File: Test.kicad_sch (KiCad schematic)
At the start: 1 part, among them U1 14528

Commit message: Updated KiCad project files with new changes
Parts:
- removed U1: 14528, symbol 4xxx:14528
- added U1, U10, U3, U4, U5, U6, U7, U8, U9: ADG1207YCPZ-REEL7, CP_32_2_ADI, symbol ADG_new:ADG1207YCPZ-REEL7
- added U2: ADL5308ACCZ, CC-14-4_ADI, symbol ADL_new:ADL5308ACCZ

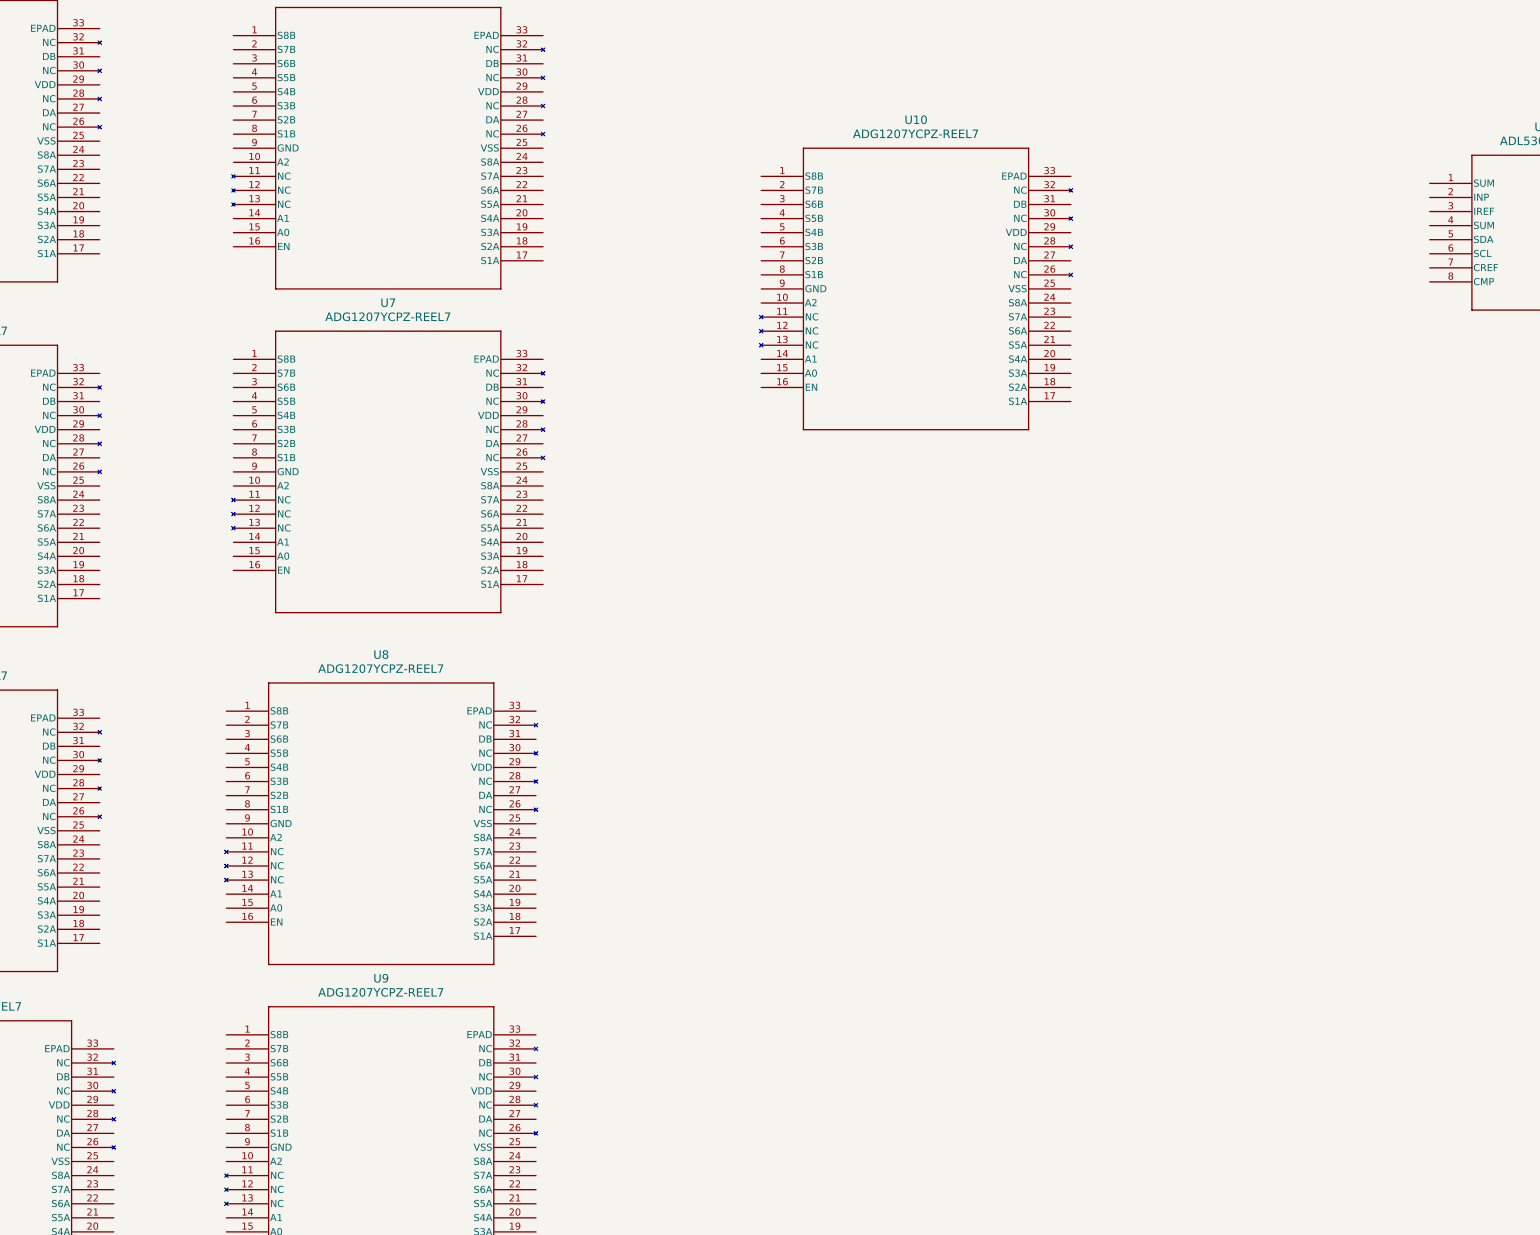
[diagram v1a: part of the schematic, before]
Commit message: new pin updates
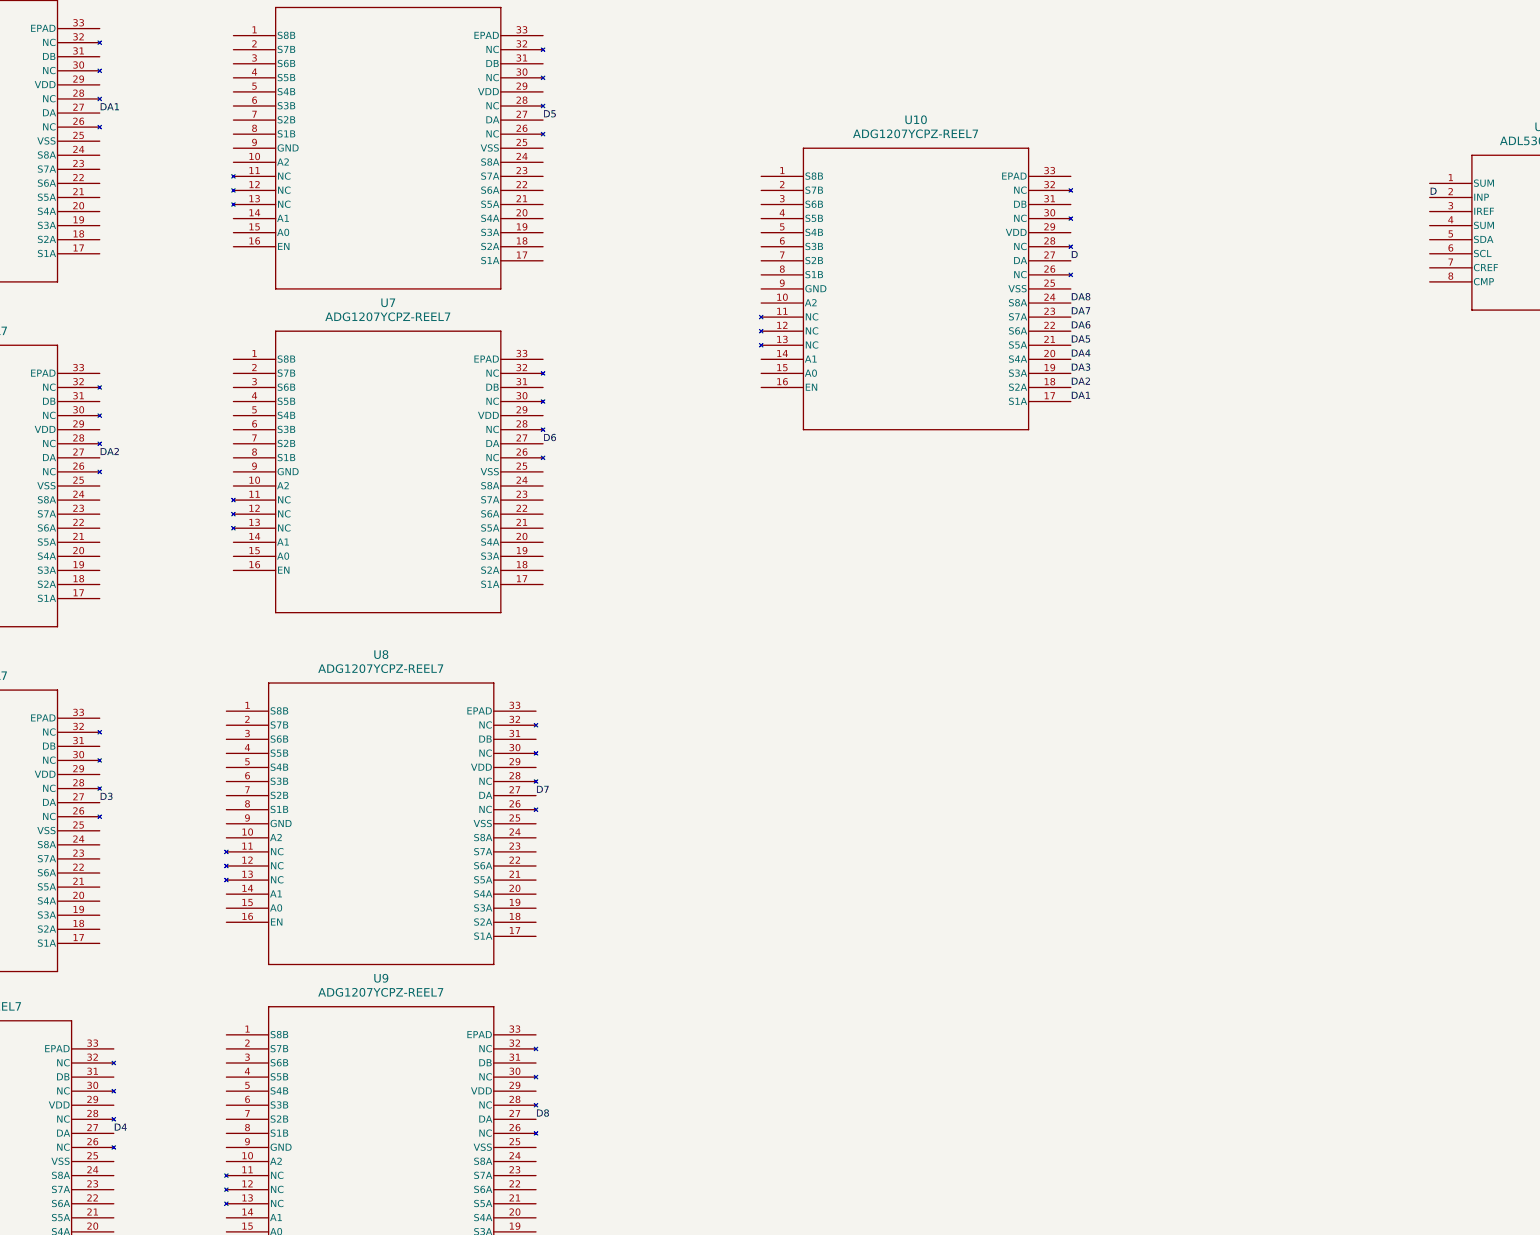
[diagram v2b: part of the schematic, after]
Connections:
- net DA1: now reaches U1.27 (DA)
- net DA1: now also U10.17 (S1A)
- net D5: now reaches U6.27 (DA)
- net D7: now reaches U8.27 (DA)
- net D3: now reaches U4.27 (DA)
- net DA2: now reaches U3.27 (DA)
- net DA2: now also U10.18 (S2A)
- net D8: now reaches U9.27 (DA)
- net DA3: now reaches U10.19 (S3A)
- net DA4: now reaches U10.20 (S4A)
- net DA5: now reaches U10.21 (S5A)
- net DA6: now reaches U10.22 (S6A)
- net DA7: now reaches U10.23 (S7A)
- net DA8: now reaches U10.24 (S8A)
- net D: now reaches U10.27 (DA)
- net D: now also U2.2 (INP)
- net D4: now reaches U5.27 (DA)
- net D6: now reaches U7.27 (DA)
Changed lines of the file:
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@@
 (kicad_sch (version 20230121) (generator eeschema)
   (paper "A2")
+  (label "D8" (at 171.45 223.52 0) (fields_autoplaced)
+    (effects (font (size 1.27 1.27)) (justify left bottom))
+  )
+  (label "DA4" (at 267.97 86.36 0) (fields_autoplaced)
+    (effects (font (size 1.27 1.27)) (justify left bottom))
+  )
+  (label "DA7" (at 267.97 78.74 0) (fields_autoplaced)
+    (effects (font (size 1.27 1.27)) (justify left bottom))
+  )
+  (label "D3" (at 92.71 166.37 0) (fields_autoplaced)
+    (effects (font (size 1.27 1.27)) (justify left bottom))
+  )
+  (label "DA8" (at 267.97 76.2 0) (fields_autoplaced)
+    (effects (font (size 1.27 1.27)) (justify left bottom))
+  )
+  (label "D4" (at 95.25 226.06 0) (fields_autoplaced)
+    (effects (font (size 1.27 1.27)) (justify left bottom))
+  )
+  (label "D5" (at 172.72 43.18 0) (fields_autoplaced)
+    (effects (font (size 1.27 1.27)) (justify left bottom))
+  )
+  (label "DA2" (at 267.97 91.44 0) (fields_autoplaced)
+    (effects (font (size 1.27 1.27)) (justify left bottom))
+  )
+  (label "DA6" (at 267.97 81.28 0) (fields_autoplaced)
+    (effects (font (size 1.27 1.27)) (justify left bottom))
+  )
+  (label "D7" (at 171.45 165.1 0) (fields_autoplaced)
+    (effects (font (size 1.27 1.27)) (justify left bottom))
+  )
+  (label "DA1" (at 92.71 41.91 0) (fields_autoplaced)
+    (effects (font (size 1.27 1.27)) (justify left bottom))
+  )
+  (label "D" (at 332.74 57.15 0) (fields_autoplaced)
+    (effects (font (size 1.27 1.27)) (justify left bottom))
+  )
+  (label "D" (at 267.97 68.58 0) (fields_autoplaced)
+    (effects (font (size 1.27 1.27)) (justify left bottom))
+  )
+  (label "DA1" (at 267.97 93.98 0) (fields_autoplaced)
+    (effects (font (size 1.27 1.27)) (justify left bottom))
+  )
+  (label "D6" (at 172.72 101.6 0) (fields_autoplaced)
+    (effects (font (size 1.27 1.27)) (justify left bottom))
+  )
+  (label "DA5" (at 267.97 83.82 0) (fields_autoplaced)
+    (effects (font (size 1.27 1.27)) (justify left bottom))
+  )
+  (label "DA3" (at 267.97 88.9 0) (fields_autoplaced)
+    (effects (font (size 1.27 1.27)) (justify left bottom))
+  )
+  (label "DA2" (at 92.71 104.14 0) (fields_autoplaced)
+    (effects (font (size 1.27 1.27)) (justify left bottom))
+  )
   (symbol (lib_id "ADG_new:ADG1207YCPZ-REEL7") (at 36.83 26.67 0) (unit 1)
     (in_bom yes) (on_board yes) (dnp no) (fields_autoplaced)

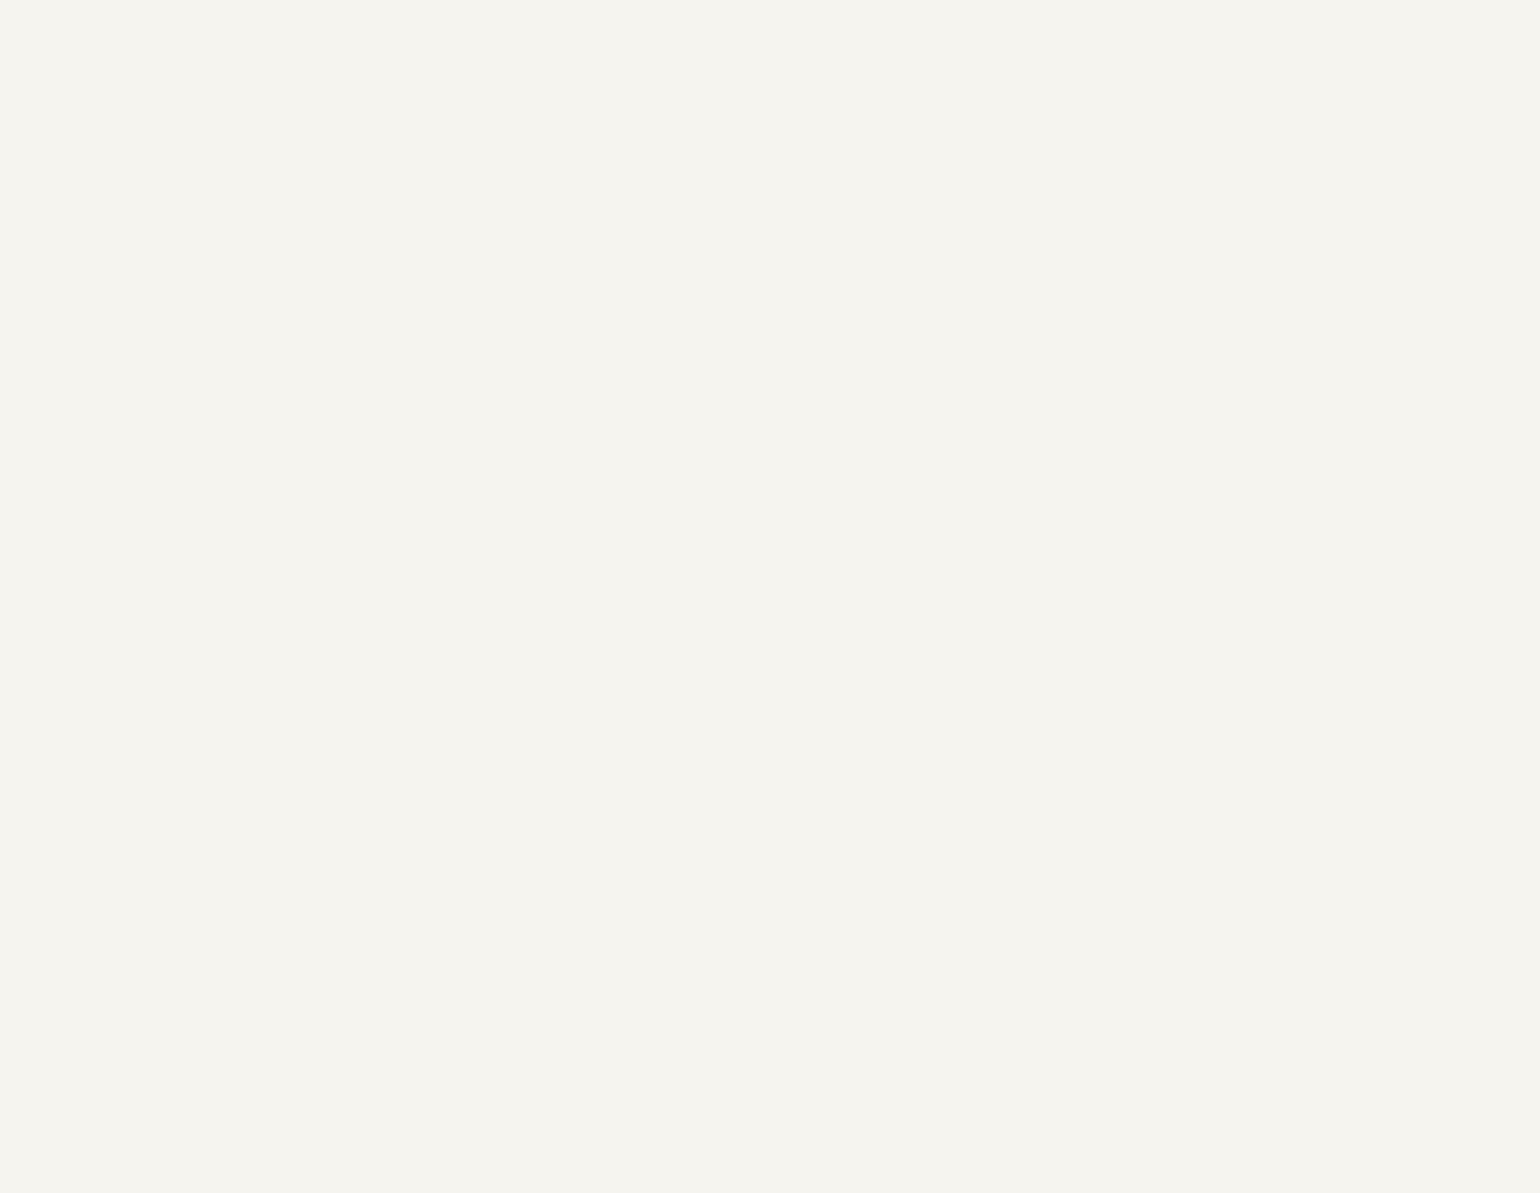
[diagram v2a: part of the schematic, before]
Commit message: Added microcontroller and LCD connections in 'test'
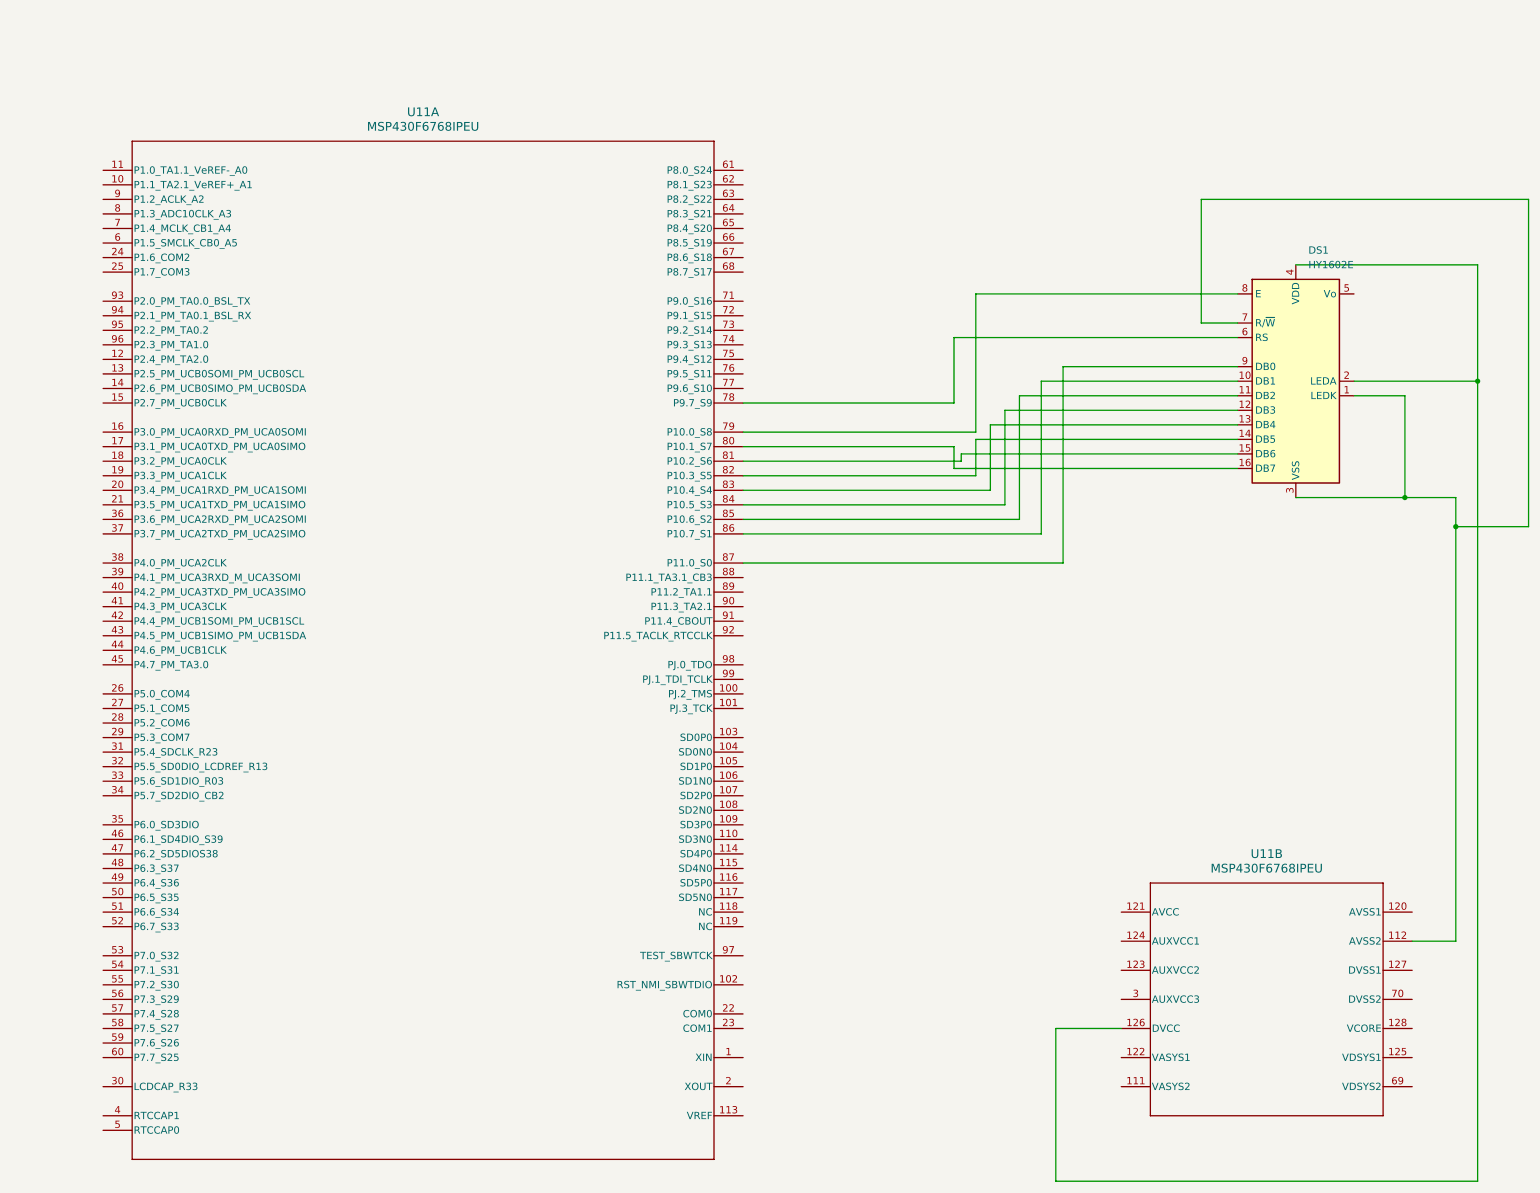
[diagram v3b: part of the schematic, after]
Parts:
- added DS1: HY1602E, Display:HY1602E, symbol Display_Character:HY1602E
- added U11: MSP430F6768IPEU, PEU0128A_N, symbol 2024-01-29_18-17-03:MSP430F6768IPEU
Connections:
- new net: DS1.6 (RS), U11.78 (P9.7_S9)
- new net: DS1.8 (E), U11.79 (P10.0_S8)
- new net: DS1.16 (DB7), U11.80 (P10.1_S7)
- new net: DS1.15 (DB6), U11.81 (P10.2_S6)
- new net: DS1.14 (DB5), U11.82 (P10.3_S5)
- new net: DS1.13 (DB4), U11.83 (P10.4_S4)
- new net: DS1.12 (DB3), U11.84 (P10.5_S3)
- new net: DS1.11 (DB2), U11.85 (P10.6_S2)
- new net: DS1.10 (DB1), U11.86 (P10.7_S1)
- new net: DS1.9 (DB0), U11.87 (P11.0_S0)
- new net: DS1.1 (LEDK), DS1.3 (VSS), DS1.7 (R/~{W}), U11.112 (AVSS2)
- new net: DS1.2 (LEDA), DS1.4 (VDD), U11.126 (DVCC)
